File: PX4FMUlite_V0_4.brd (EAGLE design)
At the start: 48.6 x 34.9 mm, 126 parts, among them J2 DF13-4P-1.25V, J201 DF13C-6P-1.25V, J202 DF13C-6P-1.25V, J203 DF13C-6P-1.25V, J3 DF13C-4P-1.25V, J302 DF13C-4P-1.25V, J401 DF13C-4P-1.25V, J403 DF13C-7P-1.25V, J405 DF13C-4P-1.25V, J802 DF13C-3P-1.25V, M3_MOUNT1101 MOUNT-HOLE3.1MM, M3_MOUNT1102 MOUNT-HOLE3.1MM, M3_MOUNT1103 MOUNT-HOLE3.1MM, M3_MOUNT1104 MOUNT-HOLE3.1MM, U101 STM32F4X7VX, U2 MAX3051, U401 MAX3051, X101 3.2x2.5 mm / 24 MHz / 15 ppm

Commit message: Tweaks tweaks
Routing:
- net N$28: track 15.5 -> 9.54 mm
- net N$48: track 18.2 -> 13.9 mm
- net FMU-VDD_3V3: track 84.6 -> 85.8 mm, vias 11 -> 14
- net CAN2_RX: track 0.00 -> 0.81 mm, vias 0 -> 1
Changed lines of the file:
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@@
 <layer number="17" name="Pads" color="2" fill="1" visible="yes" active="yes"/>
 <layer number="18" name="Vias" color="2" fill="1" visible="yes" active="yes"/>
-<layer number="19" name="Unrouted" color="14" fill="1" visible="yes" active="yes"/>
+<layer number="19" name="Unrouted" color="14" fill="1" visible="no" active="yes"/>
 <layer number="20" name="Dimension" color="15" fill="1" visible="yes" active="yes"/>
 <layer number="21" name="tPlace" color="7" fill="1" visible="yes" active="yes"/>
@@
 <wire x1="39.4208" y1="31.2928" x2="39.4208" y2="33.02" width="0.6096" layer="1"/>
 <wire x1="39.4208" y1="33.02" x2="39.7256" y2="33.3248" width="0.6096" layer="1"/>
-<wire x1="39.7256" y1="33.3248" x2="39.7256" y2="36.4744" width="0.6096" layer="1"/>
-<wire x1="39.7256" y1="36.4744" x2="39.116" y2="37.084" width="0.6096" layer="1"/>
-<wire x1="39.116" y1="37.084" x2="37.592" y2="37.084" width="0.6096" layer="1"/>
-<wire x1="37.592" y1="37.084" x2="35.9664" y2="37.084" width="0.4064" layer="1"/>
-<wire x1="35.9664" y1="37.084" x2="27.2288" y2="37.084" width="0.6096" layer="1"/>
-<wire x1="27.2288" y1="37.084" x2="25.7048" y2="37.084" width="0.4064" layer="1"/>
-<wire x1="25.7048" y1="37.084" x2="21.7424" y2="37.084" width="0.6096" layer="1"/>
-<wire x1="21.7424" y1="37.084" x2="21.4376" y2="36.7792" width="0.6096" layer="1"/>
-<wire x1="21.4376" y1="36.7792" x2="21.4376" y2="35.1536" width="0.6096" layer="1"/>
-<wire x1="21.4376" y1="35.1536" x2="21.6408" y2="34.9504" width="0.6096" layer="1"/>
-<wire x1="21.6408" y1="34.9504" x2="21.7424" y2="34.9504" width="0.6096" layer="1"/>
-<wire x1="21.7424" y1="34.9504" x2="21.7626" y2="34.9302" width="0.3048" layer="1"/>
-<wire x1="21.7626" y1="34.9302" x2="22.8026" y2="34.9302" width="0.3048" layer="1"/>
+<wire x1="39.7256" y1="33.3248" x2="39.7256" y2="36.6776" width="0.6096" layer="1"/>
 <via x="38.8112" y="30.6832" extent="1-16" drill="0.3"/>
 <via x="38.3032" y="30.6832" extent="1-16" drill="0.3"/>
@@
 <wire x1="39.360128125" y1="10.8712" x2="40.52611875" y2="9.705209375" width="0.254" layer="1"/>
 <wire x1="37.2872" y1="11.3792" x2="37.592" y2="11.684" width="0.254" layer="1"/>
-<wire x1="23.884" y1="32.1056" x2="23.884" y2="33.1216" width="0.4064" layer="1"/>
+<wire x1="23.884" y1="32.1056" x2="23.884" y2="32.6136" width="0.4064" layer="1"/>
+<wire x1="23.884" y1="32.6136" x2="23.884" y2="33.1216" width="0.4064" layer="1"/>
 <wire x1="34.4424" y1="33.1216" x2="34.4424" y2="32.6136" width="0.4064" layer="1"/>
 <wire x1="34.4424" y1="32.6136" x2="34.8488" y2="32.2072" width="0.4064" layer="1"/>
@@
 <wire x1="27.2288" y1="19.1944" x2="27.948" y2="19.1944" width="0.254" layer="16"/>
 <wire x1="27.948" y1="19.1944" x2="28.0416" y2="19.1008" width="0.254" layer="16"/>
+<wire x1="39.7256" y1="36.6776" x2="40.0304" y2="36.9824" width="0.6096" layer="1"/>
+<wire x1="40.0304" y1="36.9824" x2="40.8432" y2="36.9824" width="0.6096" layer="1"/>
+<via x="40.8432" y="36.9824" extent="1-16" drill="0.3"/>
+<wire x1="40.8432" y1="36.9824" x2="37.8968" y2="36.9824" width="0.6096" layer="15"/>
+<wire x1="37.8968" y1="36.9824" x2="37.7952" y2="37.084" width="0.4064" layer="15"/>
+<wire x1="37.7952" y1="37.084" x2="36.4744" y2="37.084" width="0.4064" layer="15"/>
+<wire x1="36.4744" y1="37.084" x2="36.3728" y2="36.9824" width="0.4064" layer="15"/>
+<wire x1="36.3728" y1="36.9824" x2="28.2528" y2="36.9824" width="0.6096" layer="15"/>
+<wire x1="28.2528" y1="36.9824" x2="23.884" y2="32.6136" width="0.6096" layer="15"/>
+<wire x1="23.884" y1="32.6136" x2="23.1648" y2="32.6136" width="0.6096" layer="15"/>
+<via x="22.5552" y="32.6136" extent="1-16" drill="0.3"/>
+<wire x1="23.1648" y1="32.6136" x2="22.5552" y2="32.6136" width="0.6096" layer="15"/>
+<wire x1="22.5552" y1="32.6136" x2="23.1648" y2="32.6136" width="0.4064" layer="1"/>
+<wire x1="23.1648" y1="32.6136" x2="23.884" y2="32.6136" width="0.4064" layer="1"/>
 <wire x1="48.6664" y1="18.6944" x2="50.792" y2="21.2344" width="0" layer="19" extent="1-15"/>
 <wire x1="29.2916" y1="28.332" x2="27.948" y2="22.9616" width="0" layer="19" extent="1-16"/>
 <wire x1="40.3352" y1="21.844" x2="39.8190125" y2="28.79709375" width="0" layer="19" extent="1-16"/>
+<via x="23.1648" y="32.6136" extent="1-16" drill="0.3"/>
 </signal>
 <signal name="OTG_FS_DP">
@@
 <contactref element="U101" pad="51"/>
 <contactref element="U2" pad="4"/>
-<wire x1="22.8026" y1="34.2802" x2="48.30429375" y2="20.3118125" width="0" layer="19" extent="1-1"/>
+<wire x1="22.8026" y1="34.2802" x2="22.7584" y2="34.2802" width="0.4064" layer="1"/>
+<via x="22.7584" y="33.528" extent="1-16" drill="0.3"/>
+<wire x1="22.7584" y1="33.528" x2="22.8026" y2="33.5722" width="0.3048" layer="1"/>
+<wire x1="22.8026" y1="33.5722" x2="22.8026" y2="34.2802" width="0.3048" layer="1"/>
+<wire x1="22.8026" y1="33.5722" x2="48.30429375" y2="20.3118125" width="0" layer="19" extent="1-1"/>
 </signal>
 <signal name="CAN2_TX">
@@
 <contactref element="R408" pad="P$1"/>
 <wire x1="37.092" y1="5.588" x2="36.3728" y2="5.588" width="0.4064" layer="1"/>
-<wire x1="36.3728" y1="5.588" x2="34.5157125" y2="11.472978125" width="0" layer="19" extent="1-16"/>
 <via x="36.3728" y="5.588" extent="1-16" drill="0.3"/>
+<wire x1="36.3728" y1="5.588" x2="34.5157125" y2="11.472978125" width="0" layer="19" extent="1-1"/>
 </signal>
 <signal name="FMU_AUX_ADC2">
@@
 <contactref element="R407" pad="P$1"/>
 <wire x1="41.648" y1="5.588" x2="42.164" y2="5.588" width="0.4064" layer="1"/>
-<wire x1="42.164" y1="5.588" x2="42.293884375" y2="11.472978125" width="0" layer="19" extent="1-16"/>
 <via x="42.164" y="5.588" extent="1-16" drill="0.3"/>
+<wire x1="42.164" y1="5.588" x2="42.293884375" y2="11.472978125" width="0" layer="19" extent="1-1"/>
 </signal>
 <signal name="N$68">
@@
 <contactref element="L403" pad="P$2"/>
 <contactref element="U$404" pad="C"/>
-<wire x1="39.3192" y1="36.6776" x2="37.8968" y2="36.6776" width="0.4064" layer="16"/>
-<wire x1="37.8968" y1="36.6776" x2="37.4904" y2="37.084" width="0.4064" layer="16"/>
-<wire x1="37.4904" y1="37.084" x2="36.4744" y2="37.084" width="0.4064" layer="16"/>
-<wire x1="36.4744" y1="37.084" x2="35.9664" y2="36.576" width="0.4064" layer="16"/>
-<wire x1="35.9664" y1="36.576" x2="33.7312" y2="36.576" width="0.4064" layer="16"/>
-<wire x1="33.7312" y1="36.576" x2="33.4264" y2="36.2712" width="0.4064" layer="16"/>
-<wire x1="33.4264" y1="36.2712" x2="33.4264" y2="32.9184" width="0.4064" layer="16"/>
-<wire x1="33.4264" y1="32.9184" x2="33.4264" y2="32.8168" width="0.4064" layer="16"/>
-<wire x1="33.4264" y1="32.8168" x2="33.6296" y2="32.6136" width="0.4064" layer="16"/>
-<wire x1="33.6296" y1="32.6136" x2="34.585" y2="32.6136" width="0.4064" layer="16"/>
+<wire x1="41.6688" y1="32.6136" x2="39.8272" y2="32.6136" width="0.4064" layer="16"/>
+<wire x1="39.8272" y1="32.6136" x2="39.5224" y2="32.9184" width="0.4064" layer="16"/>
+<wire x1="39.5224" y1="32.9184" x2="39.5224" y2="34.7472" width="0.4064" layer="16"/>
+<wire x1="39.5224" y1="34.7472" x2="39.116" y2="35.1536" width="0.4064" layer="16"/>
+<wire x1="39.116" y1="35.1536" x2="34.8488" y2="35.1536" width="0.4064" layer="16"/>
+<wire x1="34.8488" y1="35.1536" x2="34.544" y2="34.8488" width="0.4064" layer="16"/>
+<wire x1="34.544" y1="34.8488" x2="34.544" y2="32.6834" width="0.4064" layer="16"/>
+<wire x1="34.544" y1="32.6834" x2="34.5994" y2="32.628" width="0.4064" layer="16"/>
+<wire x1="32.4024" y1="32.8168" x2="33.3248" y2="32.8168" width="0.4064" layer="16"/>
+<wire x1="33.3248" y1="32.8168" x2="33.528" y2="32.6136" width="0.4064" layer="16"/>
+<wire x1="33.528" y1="32.6136" x2="34.585" y2="32.6136" width="0.4064" layer="16"/>
 <wire x1="34.585" y1="32.6136" x2="34.5994" y2="32.628" width="0.4064" layer="16"/>
-<wire x1="32.4024" y1="32.8168" x2="33.3248" y2="32.8168" width="0.4064" layer="16"/>
-<wire x1="33.3248" y1="32.8168" x2="33.4264" y2="32.9184" width="0.4064" layer="16"/>
-<wire x1="39.3192" y1="36.6776" x2="39.5352" y2="36.4616" width="0.4064" layer="16"/>
-<wire x1="39.5352" y1="36.4616" x2="39.5224" y2="36.4616" width="0.4064" layer="16"/>
-<wire x1="39.5224" y1="36.4616" x2="39.5224" y2="33.1216" width="0.4064" layer="16"/>
-<wire x1="39.5224" y1="33.1216" x2="40.0304" y2="32.6136" width="0.4064" layer="16"/>
-<wire x1="40.0304" y1="32.6136" x2="41.6688" y2="32.6136" width="0.4064" layer="16"/>
 </signal>
 <signal name="5V_S3_FILTERED" class="1">
@@
 <contactref element="L7" pad="P$2"/>
 <contactref element="U$7" pad="C"/>
-<wire x1="28.956" y1="33.0072" x2="28.956" y2="35.9664" width="0.4064" layer="16"/>
-<wire x1="28.956" y1="35.9664" x2="28.448" y2="36.4744" width="0.4064" layer="16"/>
-<wire x1="28.448" y1="36.4744" x2="27.3304" y2="36.4744" width="0.4064" layer="16"/>
-<wire x1="27.3304" y1="36.4744" x2="26.7208" y2="37.084" width="0.4064" layer="16"/>
-<wire x1="26.7208" y1="37.084" x2="23.368" y2="37.084" width="0.4064" layer="16"/>
-<wire x1="23.368" y1="37.084" x2="22.7584" y2="36.4744" width="0.4064" layer="16"/>
-<wire x1="22.7584" y1="36.4744" x2="22.7584" y2="33.4264" width="0.4064" layer="16"/>
-<wire x1="22.7584" y1="33.4264" x2="23.5568" y2="32.628" width="0.4064" layer="16"/>
-<wire x1="23.5568" y1="32.628" x2="23.9314" y2="32.628" width="0.4064" layer="16"/>
 <wire x1="30.0736" y1="33.012" x2="28.9608" y2="33.012" width="0.4064" layer="16"/>
 <wire x1="28.9608" y1="33.012" x2="28.956" y2="33.0072" width="0.4064" layer="16"/>
+<wire x1="28.956" y1="33.0072" x2="28.956" y2="33.8328" width="0.4064" layer="16"/>
+<wire x1="28.956" y1="33.8328" x2="27.6352" y2="35.1536" width="0.4064" layer="16"/>
+<wire x1="27.6352" y1="35.1536" x2="24.7904" y2="35.1536" width="0.4064" layer="16"/>
+<wire x1="24.7904" y1="35.1536" x2="23.9314" y2="34.2946" width="0.4064" layer="16"/>
+<wire x1="23.9314" y1="34.2946" x2="23.9314" y2="32.628" width="0.4064" layer="16"/>
 </signal>
 <signal name="N$29">

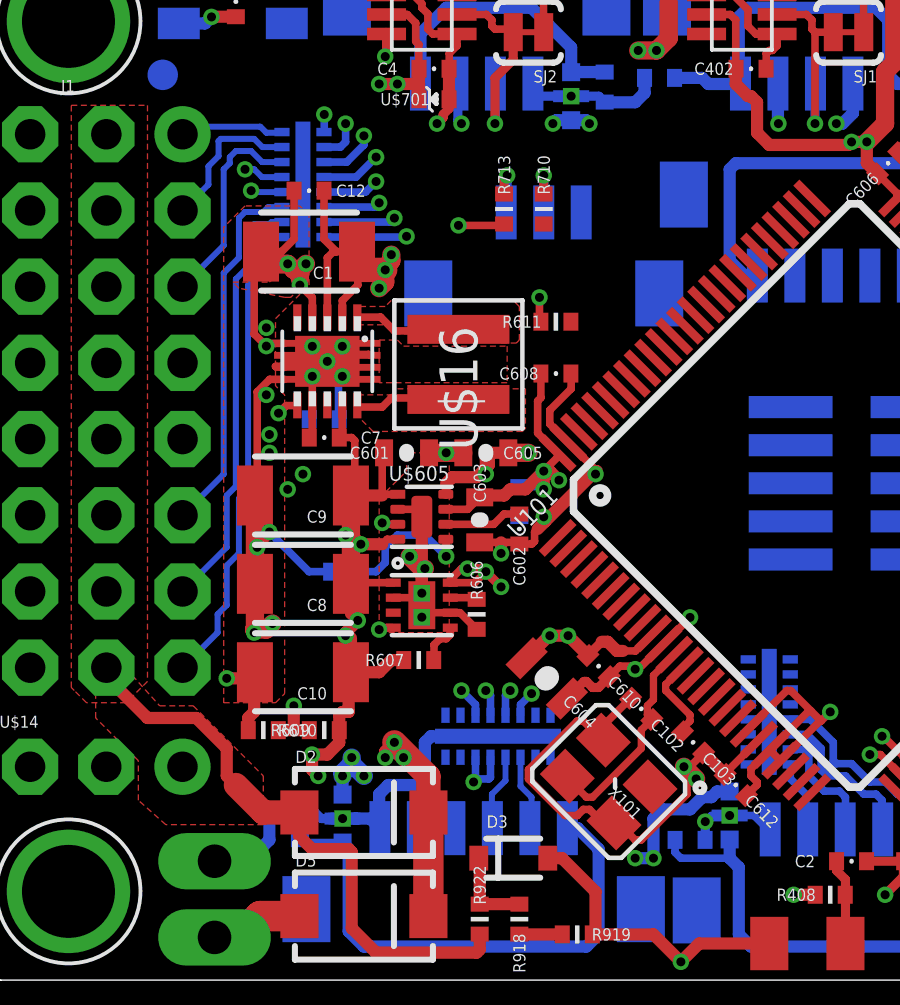
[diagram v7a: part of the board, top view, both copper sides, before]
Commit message: More pre-autoroute tweaks
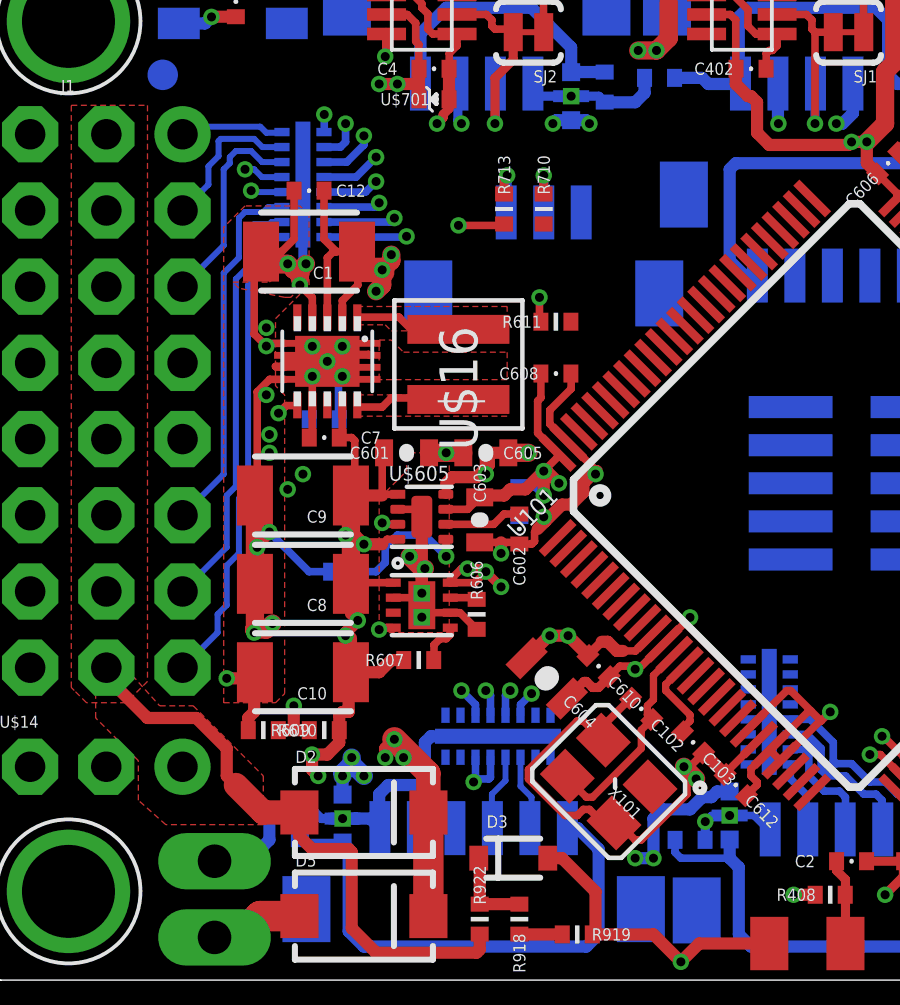
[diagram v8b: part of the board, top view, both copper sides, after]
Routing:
- net GND: track 213.8 -> 216.7 mm
- net FMU-VDD_3V3: track 85.8 -> 86.3 mm
